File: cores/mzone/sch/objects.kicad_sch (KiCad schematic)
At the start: 35 parts

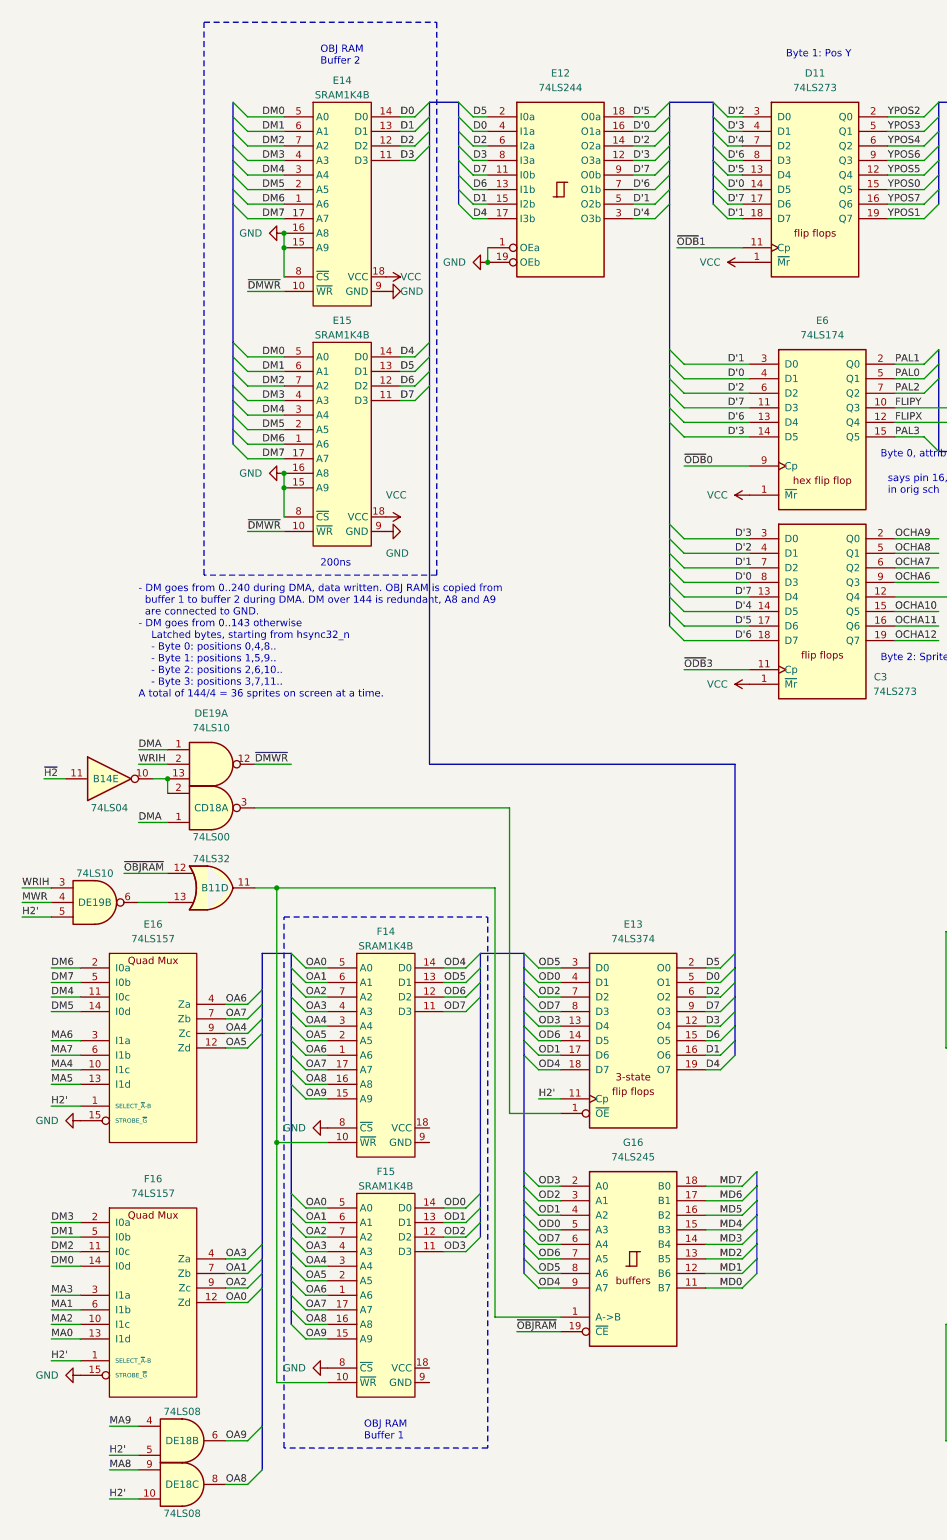
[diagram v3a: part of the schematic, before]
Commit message: mzone core
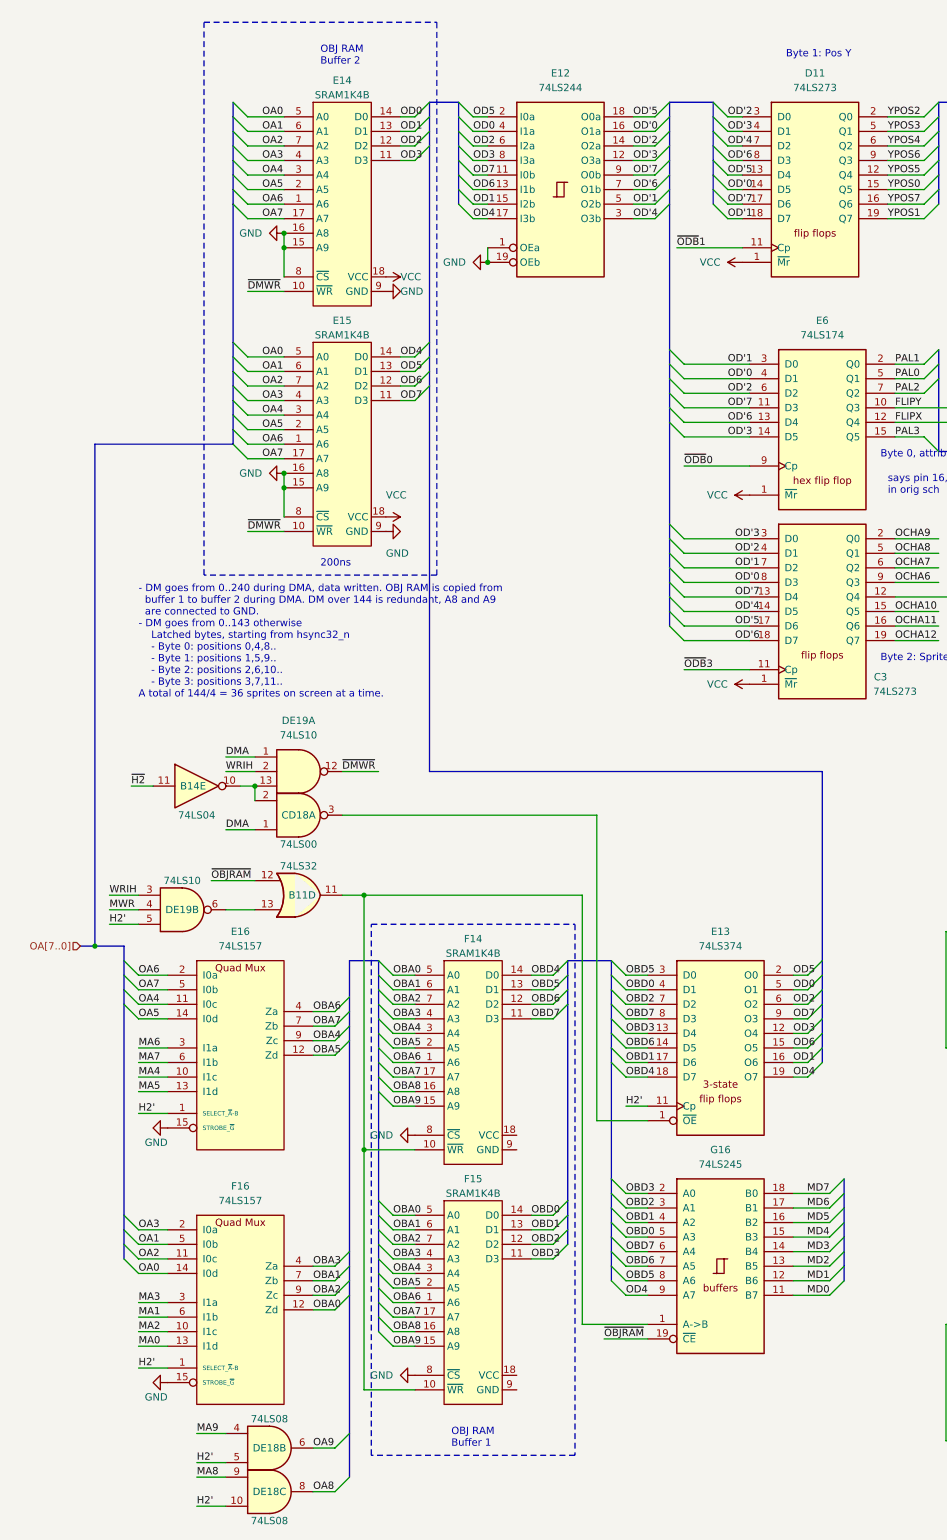
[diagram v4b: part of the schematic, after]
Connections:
- net D0 is gone; now on net OD0: E12.4 (I1a), E13.5 (O1), E14.14 (D0)
- net D1 is gone; now on net OD1: E12.15 (I2b), E13.16 (O6), E14.13 (D1)
- net D2 is gone; now on net OD2: E12.6 (I2a), E13.6 (O2), E14.12 (D2)
- net D3 is gone; now on net OD3: E12.8 (I3a), E13.12 (O4), E14.11 (D3)
- net D4 is gone; now on net OD4: E12.17 (I3b), E13.19 (O7), E15.14 (D0)
- net D5 is gone; now on net OD5: E12.2 (I0a), E13.2 (O0), E15.13 (D1)
- net D6 is gone; now on net OD6: E12.13 (I1b), E13.15 (O5), E15.12 (D2)
- net D7 is gone; now on net OD7: E12.11 (I0b), E13.9 (O3), E15.11 (D3)
- net DM0 is gone; now on net OA0: E14.5 (A0), E15.5 (A0), F16.14 (I0d)
- net DM1 is gone; now on net OA1: E14.6 (A1), E15.6 (A1), F16.5 (I0b)
- net DM2 is gone; now on net OA2: E14.7 (A2), E15.7 (A2), F16.11 (I0c)
- net DM3 is gone; now on net OA3: E14.4 (A3), E15.4 (A3), F16.2 (I0a)
- net DM4 is gone; now on net OA4: E14.3 (A4), E15.3 (A4), E16.11 (I0c)
- net DM5 is gone; now on net OA5: E14.2 (A5), E15.2 (A5), E16.14 (I0d)
- net DM6 is gone; now on net OA6: E14.1 (A6), E15.1 (A6), E16.2 (I0a)
- net DM7 is gone; now on net OA7: E14.17 (A7), E15.17 (A7), E16.5 (I0b)
- net D'0: no longer C3.8 (D3), D11.14 (D5), E12.16 (O1a), E6.4 (D1)
- net D'1: no longer C3.7 (D2), D11.18 (D7), E12.5 (O2b), E6.3 (D0)
- net D'2: no longer C3.4 (D1), D11.3 (D0), E12.14 (O2a), E6.6 (D2)
- net D'3: no longer C3.3 (D0), D11.4 (D1), E12.12 (O3a), E6.14 (D5)
- net D'4: no longer C3.14 (D5), D11.7 (D2), E12.3 (O3b)
- net D'5: no longer C3.17 (D6), D11.13 (D4), E12.18 (O0a)
- net D'6: no longer C3.18 (D7), D11.8 (D3), E12.7 (O1b), E6.13 (D4)
- net D'7: no longer C3.13 (D4), D11.17 (D6), E12.9 (O0b), E6.11 (D3)
- net OA0: no longer F14.5 (A0), F15.5 (A0), F16.12 (Zd)
- net OA1: no longer F14.6 (A1), F15.6 (A1), F16.7 (Zb)
- net OA2: no longer F14.7 (A2), F15.7 (A2), F16.9 (Zc)
- net OA3: no longer F14.4 (A3), F15.4 (A3), F16.4 (Za)
- net OA4: no longer E16.9 (Zc), F14.3 (A4), F15.3 (A4)
- net OA5: no longer E16.12 (Zd), F14.2 (A5), F15.2 (A5)
- net OA6: no longer E16.4 (Za), F14.1 (A6), F15.1 (A6)
- net OA7: no longer E16.7 (Zb), F14.17 (A7), F15.17 (A7)
- net OA8: no longer F14.16 (A8), F15.16 (A8)
- net OA9: no longer F14.15 (A9), F15.15 (A9)
- net OD0: no longer E13.4 (D1), F15.14 (D0), G16.5 (A3)
- net OD1: no longer E13.17 (D6), F15.13 (D1), G16.4 (A2)
- net OD2: no longer E13.7 (D2), F15.12 (D2), G16.3 (A1)
- net OD3: no longer E13.13 (D4), F15.11 (D3), G16.2 (A0)
- net OD4: no longer E13.18 (D7), F14.14 (D0)
- net OD5: no longer E13.3 (D0), F14.13 (D1), G16.8 (A6)
- net OD6: no longer E13.14 (D5), F14.12 (D2), G16.7 (A5)
- net OD7: no longer E13.8 (D3), F14.11 (D3), G16.6 (A4)
- new net OBA0: F14.5 (A0), F15.5 (A0), F16.12 (Zd)
- new net OBA1: F14.6 (A1), F15.6 (A1), F16.7 (Zb)
- new net OBA2: F14.7 (A2), F15.7 (A2), F16.9 (Zc)
- new net OBA3: F14.4 (A3), F15.4 (A3), F16.4 (Za)
- new net OBA4: E16.9 (Zc), F14.3 (A4), F15.3 (A4)
- new net OBA5: E16.12 (Zd), F14.2 (A5), F15.2 (A5)
- new net OBA6: E16.4 (Za), F14.1 (A6), F15.1 (A6)
- new net OBA7: E16.7 (Zb), F14.17 (A7), F15.17 (A7)
- new net OBA8: F14.16 (A8), F15.16 (A8)
- new net OBA9: F14.15 (A9), F15.15 (A9)
- new net OBD0: E13.4 (D1), F15.14 (D0), G16.5 (A3)
- new net OBD1: E13.17 (D6), F15.13 (D1), G16.4 (A2)
- new net OBD2: E13.7 (D2), F15.12 (D2), G16.3 (A1)
- new net OBD3: E13.13 (D4), F15.11 (D3), G16.2 (A0)
- new net OBD4: E13.18 (D7), F14.14 (D0)
- new net OBD5: E13.3 (D0), F14.13 (D1), G16.8 (A6)
- new net OBD6: E13.14 (D5), F14.12 (D2), G16.7 (A5)
- new net OBD7: E13.8 (D3), F14.11 (D3), G16.6 (A4)
- new net OD'0: C3.8 (D3), D11.14 (D5), E12.16 (O1a), E6.4 (D1)
- new net OD'1: C3.7 (D2), D11.18 (D7), E12.5 (O2b), E6.3 (D0)
- new net OD'2: C3.4 (D1), D11.3 (D0), E12.14 (O2a), E6.6 (D2)
- new net OD'3: C3.3 (D0), D11.4 (D1), E12.12 (O3a), E6.14 (D5)
- new net OD'4: C3.14 (D5), D11.7 (D2), E12.3 (O3b)
- new net OD'5: C3.17 (D6), D11.13 (D4), E12.18 (O0a)
- new net OD'6: C3.18 (D7), D11.8 (D3), E12.7 (O1b), E6.13 (D4)
- new net OD'7: C3.13 (D4), D11.17 (D6), E12.9 (O0b), E6.11 (D3)
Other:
- moved on the sheet: B11D, B14E, CD18A, DE18B, DE18C, DE19A, DE19B, E13, E16, F14, F15, F16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

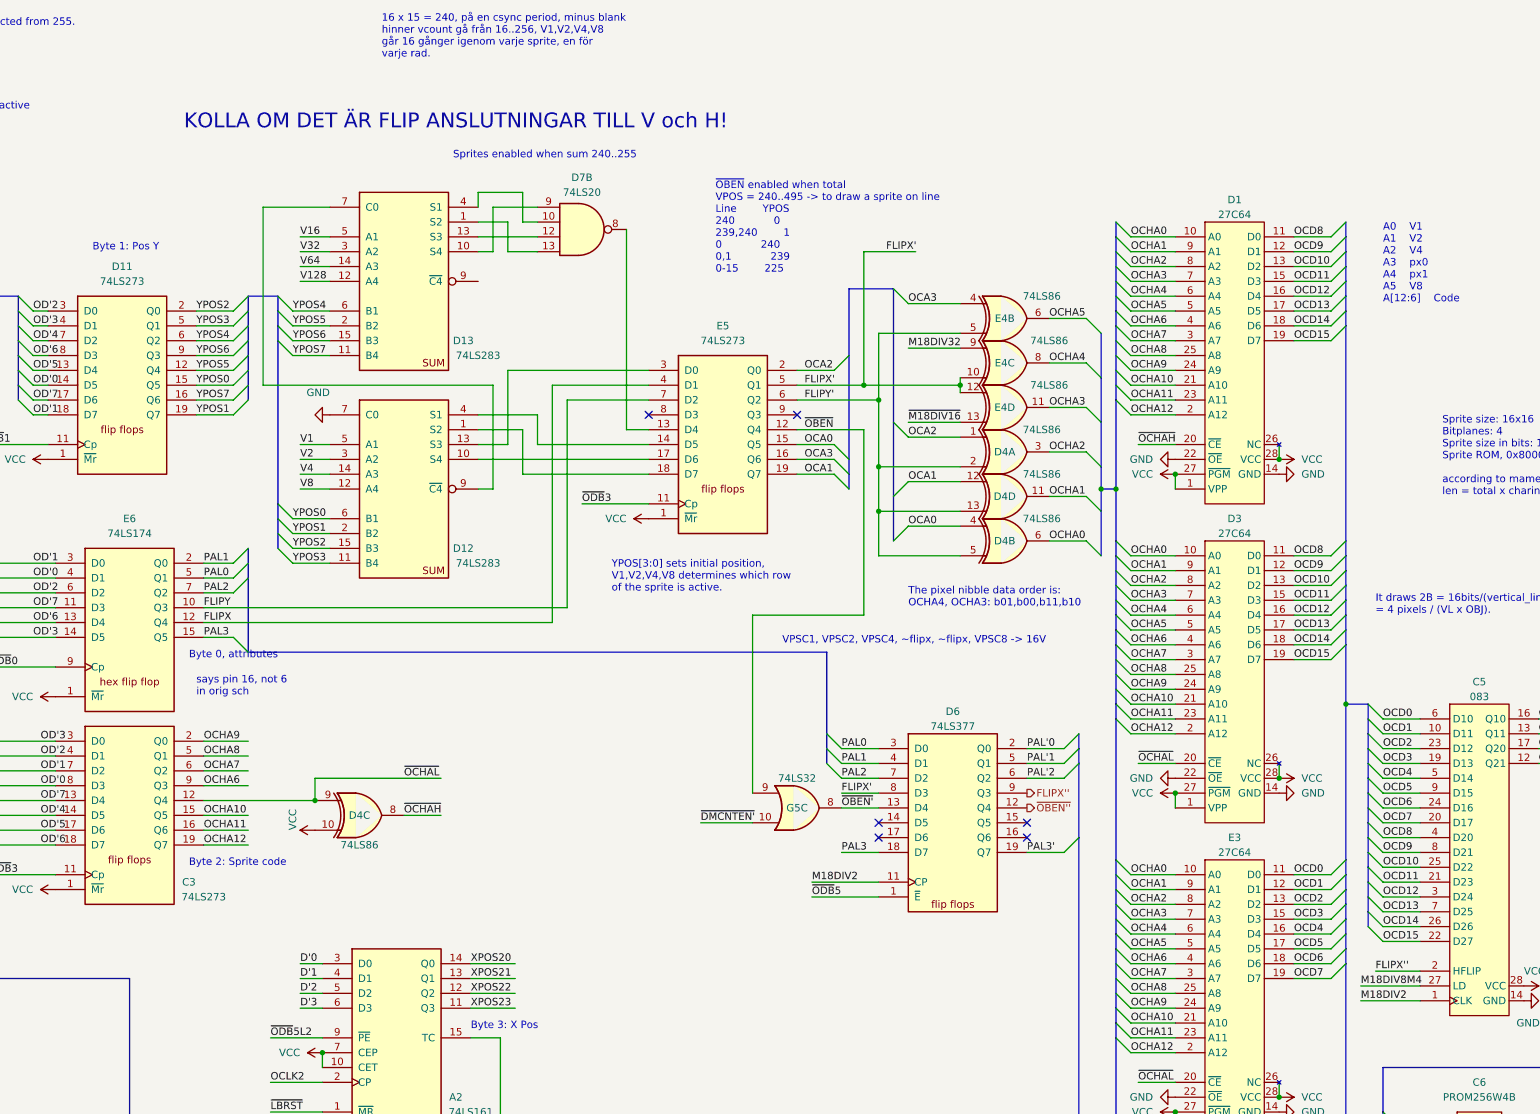
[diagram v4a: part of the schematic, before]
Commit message: mzone core
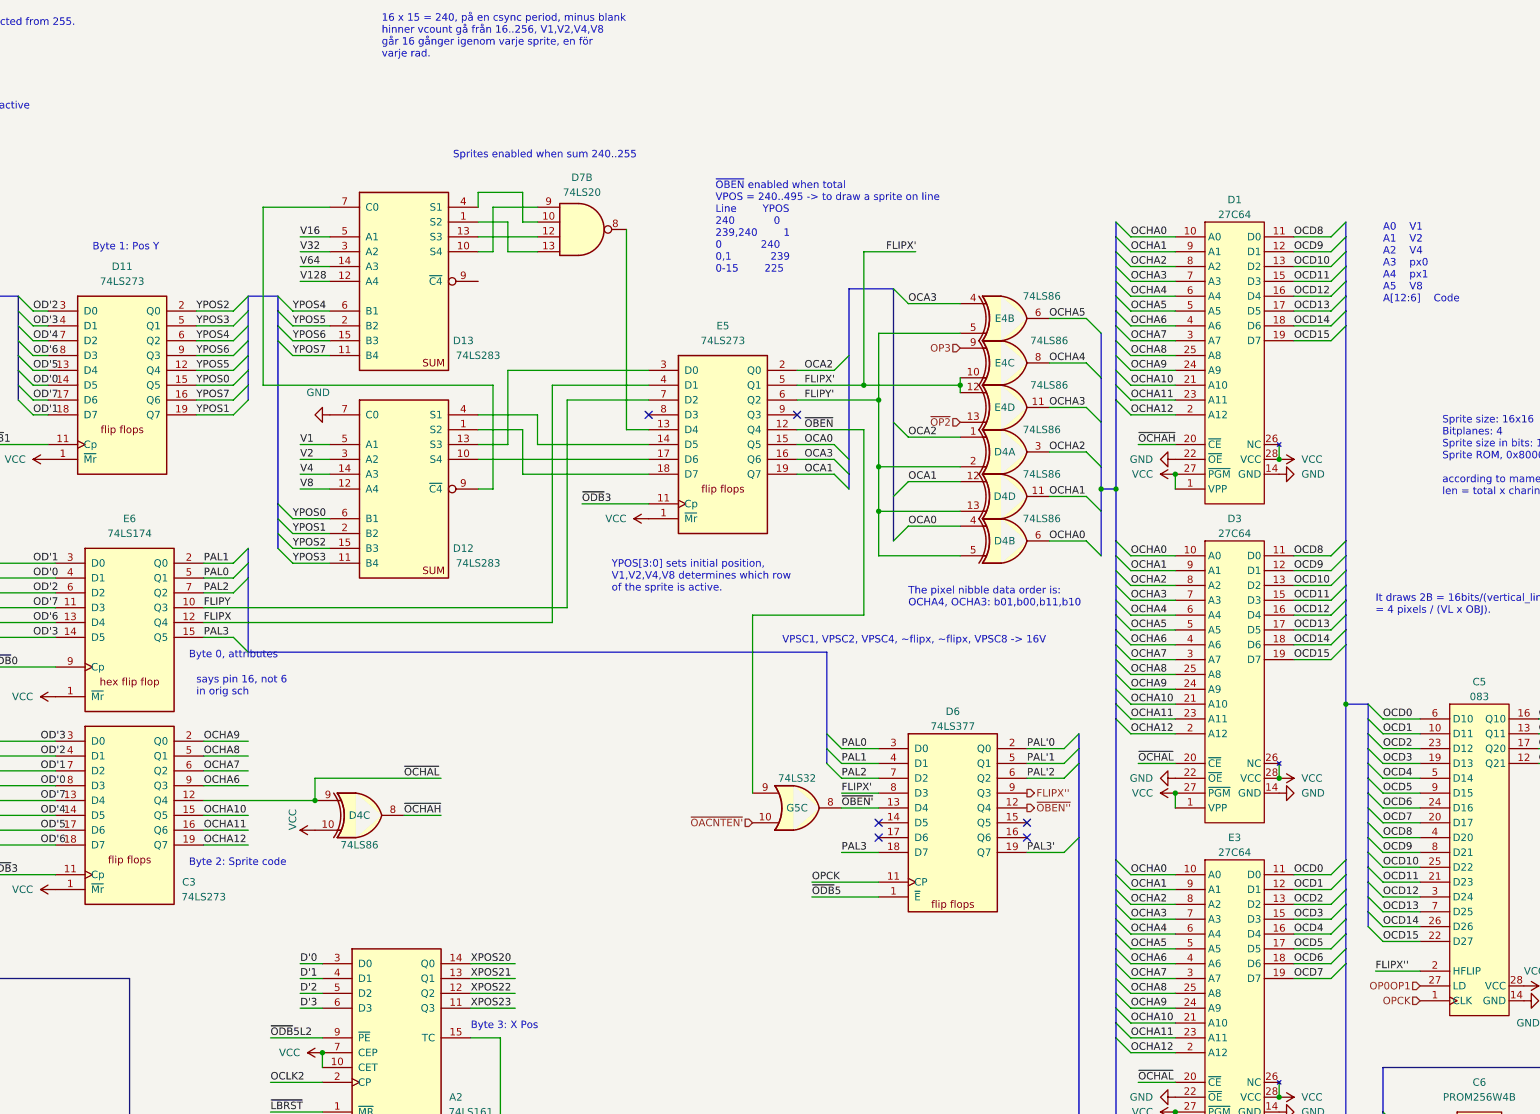
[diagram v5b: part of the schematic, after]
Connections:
- net M18DIV2 renamed OPCK
- net M18DIV32 renamed OP3
- net M18DIV8M4 renamed OP0OP1
- net ~{DMCNTEN'} renamed ~{OACNTEN'}
- net ~{M18DIV16} renamed ~{OP2}
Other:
- note removed: "KOLLA OM DET ÄR FLIP ANSLUTNINGAR TILL V och H!"

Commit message: mzone core
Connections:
- net D'0 is gone; now on net OD'0: A2.3 (D0), B2.3 (D0)
- net D'1 is gone; now on net OD'1: A2.4 (D1), B2.4 (D1)
- net D'2 is gone; now on net OD'2: A2.5 (D2), B2.5 (D2)
- net D'3 is gone; now on net OD'3: A2.6 (D3), B2.6 (D3)
- net D'4 is gone; now on net OD'4: A3.3 (D0), B3.3 (D0)
- net D'5 is gone; now on net OD'5: A3.4 (D1), B3.4 (D1)
- net D'6 is gone; now on net OD'6: A3.5 (D2), B3.5 (D2)
- net D'7 is gone; now on net OD'7: A3.6 (D3), B3.6 (D3)
- net OA8 is gone; now on net OBA8: DE18.8
- net OA9 is gone; now on net OBA9: DE18.6
- net GND: now also C6.8 (GND), F14.9 (GND), F15.9 (GND)
- net VCC: now also C6.16 (VCC), F14.18 (VCC), F15.18 (VCC)
- net MA0 renamed MA'0
- net MA1 renamed MA'1
- net MA2 renamed MA'2
- net MA3 renamed MA'3
- net MA4 renamed MA'4
- net MA5 renamed MA'5
- net MA6 renamed MA'6
- net MA7 renamed MA'7
- net MA8 renamed MA'8
- net MA9 renamed MA'9
- net ~{ODB}5L1 renamed ~{ODB5L}1
- net ~{ODB}5L2 renamed ~{ODB5L}2
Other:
- note added: "- DM goes from 0..240 during DMA, data written. OBJ RAM is copied from buffer 1 to buffer 2 during DMA. DM over 144 is redundant, A8 and A9 are connected to GND. - DM goes from 0..143 otherwise A total of 144/4 = 36 sprites on screen at a time."
- note added: "When the corresponding line counter is enabled ,~{ODB5L}1 or ~{ODB5L}2, the x positions go from 0..15, drawing every pixel of the 16 x 16 sprite object to the active line buffer for drawing. When the line buffer toggles after ~{LBRST} goes high the pixels are read and the x positions go from 0..239 during scroll/obj layers active."
- note removed: "- DM goes from 0..240 during DMA, data written. OBJ RAM is copied from buffer 1 to buffer 2 during DMA. DM over 144 is redundant, A8 and A9 are connected to GND. - DM goes from 0..143 otherwise Latched bytes, starting from hsync32_n - Byte 0: positions 0,4,8.. - Byte 1: positions 1,5,9.. - Byte 2: positions 2,6,10.. - Byte 3: positions 3,7,11.. A total of 144/4 = 36 sprites on screen at a time."
- note removed: "128 + 64 +32 + 16 = 240 16 x 15 = 240, på en csync period, minus blank hinner vcount gå från 16..256, V1,V2,V4,V8 går 16 gånger igenom varje sprite, en för varje rad."
- note removed: "It draws 2B = 16bits/(vertical_line x object) = 4 pixels / (VL x OBJ)."
- note removed: "Object RAM Byte 0 D[3:0] color, palette D[5:4] not used D6 flipx, inverted in mame, check D7 flipy Byte 1 Pos y, in mame 16 is added to the value and subtracted from 255. Byte 2 Sprite code Byte 3 Pos x, 32 is added to this value unless flipscreen is active"
- note removed: "Sprite size: 16x16 Bitplanes: 4 Sprite size in bits: 16px x 16px x 4b/px = 1024b/sprite = 1024b/sprite x 8b/B = 128 bytes/sprite Sprite ROM, 0x8000 = 32768B. 32768B/128B/sprite = 256sprites. according to mame charincrement is 64bytes, 64 x 8b = 512b, why? len = total x charincrement = 4b/plane x 64 x 8 = 2048b"
- note removed: "Sprites enabled when sum 240..255"
- note removed: "The pixel nibble data order is: OCHA4, OCHA3: b01,b00,b11,b10"
- note removed: "VPSC1, VPSC2, VPSC4, ~flipx, ~flipx, VPSC8 -> 16V"
- note removed: "When LD goes high it will take in two bytes. The lower byte db0 and higher db1. db0[3:0] will be shifted to dsh0[1] and db0[7:4] to dsh0[0].The lowest bit of the nibbles will go out immediately and the other bits in rising bit order will come out. The same goes for the high byte, but it comes out in dsh[1:0]. The bit order is reversed for the nibbles if HFLIP is high. When load is high and clk go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"
- note removed: "When the corresponding line counter is enabled ,~{LDCNT1}, the x positions go from 0..15, drawing every pixel of the 16 x 16 sprite object to the active line buffer for drawing. When the line buffer toggles after ~{LBRST} goes high the pixels are read and the x positions go from 0..239 during scroll/obj layers active."
- note removed: "YPOS[3:0] sets initial position, V1,V2,V4,V8 determines which row of the sprite is active."
- note removed: "dsh0[0] = Q11(16), dsh0[1] = Q10(13) dsh1[0] = Q21(17), dsh1[1] = Q20(12)"
- note removed: "says pin 16, not 6 in orig sch"
- note removed: "~{OBEN} enabled when total VPOS = 240..495 -> to draw a sprite on line Line YPOS 240 0 239,240 1 0 240 0,1 239 0-15 225"
- moved on the sheet: C5, C6, D6, DE18B, DE18C, DE19B, E13, E14, E15, E16, F16, G16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
